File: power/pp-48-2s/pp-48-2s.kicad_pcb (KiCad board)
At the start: 4 copper layers, 150 x 95 mm, 178 parts, among them J1 BUS 40-60V, J101 NODE 1, J2 CTRL IN, J201 NODE 2, J3 CTRL OUT, J4 12V AUX OUT, J5 SWD, Q1 2N7002, Q101 BSC070N10NS5, Q102 2N7002, Q103 2N7002, Q104 2N7002, Q201 BSC070N10NS5, Q202 2N7002, Q203 2N7002, Q204 2N7002, U1 LM5164DDA, U101 LM5069MM-2, U102 INA238AIDGSR, U103 74LVC1G74, U104 TLP176AM, U105 TLP176AM, U106 TLP291, U2 LM5164DDA, U201 LM5069MM-2, U202 INA238AIDGSR, U203 74LVC1G74, U204 TLP176AM, U205 TLP176AM, U206 TLP291, U3 STM32G0B1CBT6, U4 ISO1640BD, U5 ISO7721D, U6 MCP23017-E/SO, X101 PM-19V-200W, X102 J2 AUX, X201 PM-19V-200W, X202 J2 AUX, Y1 8MHz

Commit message: power: syncfields ported to KiCad 10, PP-48-2S board fields synced from the schematic
FOOTPRINT.GetFieldByName is gone in KiCad 10; use HasField / GetField /
SetField by name. Description added to the synced fields, --dry option,
per-change report. Run on the board: 108 Value / LCSC / Description
fields on 174 footprints, kicad-cli drc --schematic-parity 0 mismatches
(was 104), copper untouched, DRC the same 5 warnings.
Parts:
- C22, C23: value 12p -> 33p
- J101: value NODE 1 -> NODE
- J201: value NODE 2 -> NODE

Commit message: power: PP-48-2S plane MCU STM32G0B1CBT6 -> STM32G070CBT6 (G0B1 out of stock at LCSC; pinout checked, 8-slot S7 pins moved off the unbonded 29/32); handoff: JLC stock check
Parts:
- U3: value STM32G0B1CBT6 -> STM32G070CBT6
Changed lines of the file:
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@@
 				(font
 					(size 1.27 1.27)
+					(thickness 0.15)
 				)
 			)
@@
 			)
 		)
-		(property "Value" "STM32G0B1CBT6"
+		(property "Value" "STM32G070CBT6"
 			(at 0 5.85 0)
 			(layer "F.Fab")
@@
 			)
 		)
-		(property "LCSC" "C2847904"
+		(property "LCSC" "C529338"
 			(at 0 0 0)
 			(layer "F.Fab")
@@
 			(layers "F.Cu" "F.Mask" "F.Paste")
 			(roundrect_rratio 0.25)
-			(net "unconnected-(U3-PA9{slash}UCPD1_DBCC1-Pad29)")
+			(net "unconnected-(U3-NC{slash}PA9-Pad29)")
 		)
 		(pad "30" smd roundrect
@@
 			(layers "F.Cu" "F.Mask" "F.Paste")
 			(roundrect_rratio 0.25)
-			(net "unconnected-(U3-PA10{slash}UCPD1_DBCC2-Pad32)")
+			(net "unconnected-(U3-NC{slash}PA10-Pad32)")
 		)
 		(pad "33" smd roundrect
@@
 				(font
 					(size 1.27 1.27)
+					(thickness 0.15)
 				)
 			)
@@
 				(font
 					(size 1.27 1.27)
+					(thickness 0.15)
 				)
 			)
@@
 				(font
 					(size 1.27 1.27)
+					(thickness 0.15)
 				)
 			)

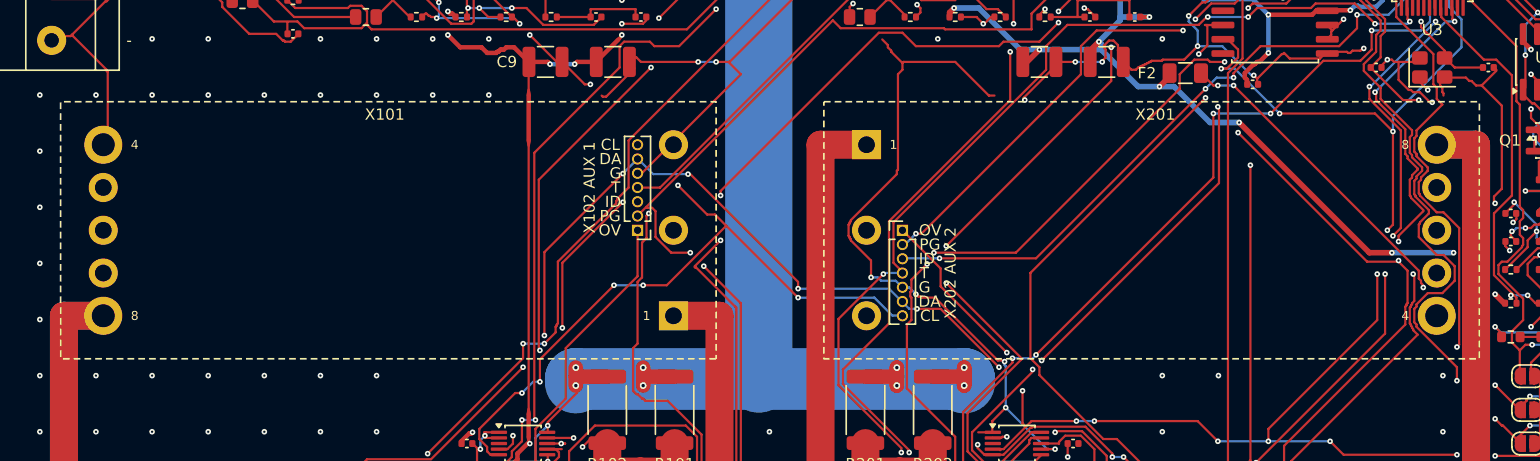
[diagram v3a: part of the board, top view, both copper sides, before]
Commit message: power: screwed PM module mount footprints (M2 into SMT standoffs, pogo aux) on module, plane and bench carrier; RUN moves to aux pad 8; copper not yet rerouted
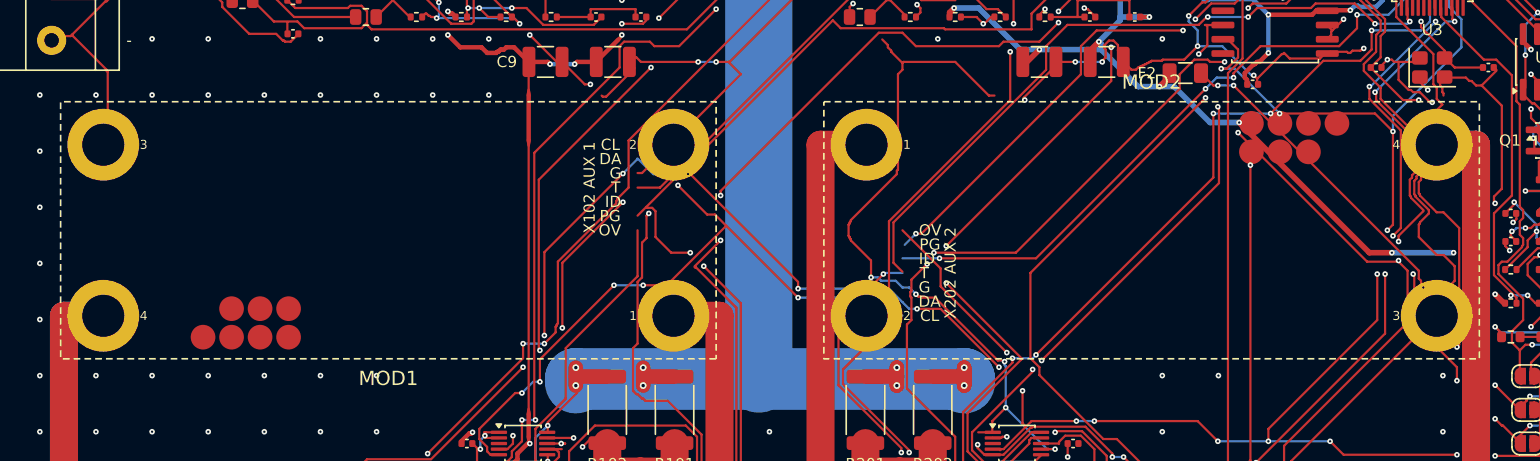
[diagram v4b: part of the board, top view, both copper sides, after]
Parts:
- removed X101, X201: PM-19V-200W, pp:Brick_Eighth_DOSA_Plane
- removed X102, X202: J2 AUX, Connector_PinHeader_1.27mm:PinHeader_1x07_P1.27mm_Vertical
- added MOD1: PM_Module_Outline, pp:PM_Module_Outline, F.Cu at (136.0, 137.0)
- added MOD2: PM_Module_Outline, pp:PM_Module_Outline, F.Cu at (204.0, 137.0)
- added PG101: pogo, pp:PM_Pogo_YZ130115073P, F.Cu at (127.1, 146.5)
- added PG102: pogo, pp:PM_Pogo_YZ130115073P, F.Cu at (124.6, 146.5)
- added PG103: pogo, pp:PM_Pogo_YZ130115073P, F.Cu at (122.0, 146.5)
- added PG104: pogo, pp:PM_Pogo_YZ130115073P, F.Cu at (119.5, 146.5)
- added PG105: pogo, pp:PM_Pogo_YZ130115073P, F.Cu at (127.1, 144.0)
- added PG106: pogo, pp:PM_Pogo_YZ130115073P, F.Cu at (124.6, 144.0)
- added PG107: pogo, pp:PM_Pogo_YZ130115073P, F.Cu at (122.0, 144.0)
- added PG201: pogo, pp:PM_Pogo_YZ130115073P, F.Cu at (212.9, 127.5)
- added PG202: pogo, pp:PM_Pogo_YZ130115073P, F.Cu at (215.4, 127.5)
- added PG203: pogo, pp:PM_Pogo_YZ130115073P, F.Cu at (218.0, 127.5)
- added PG204: pogo, pp:PM_Pogo_YZ130115073P, F.Cu at (220.5, 127.5)
- added PG205: pogo, pp:PM_Pogo_YZ130115073P, F.Cu at (212.9, 130.0)
- added PG206: pogo, pp:PM_Pogo_YZ130115073P, F.Cu at (215.4, 130.0)
- added PG207: pogo, pp:PM_Pogo_YZ130115073P, F.Cu at (218.0, 130.0)
- added SO101: M2x6 standoff, pp:PM_Standoff_M2x6_SMTSO, F.Cu at (161.4, 144.6)
- added SO102: M2x6 standoff, pp:PM_Standoff_M2x6_SMTSO, F.Cu at (161.4, 129.4)
- added SO103: M2x6 standoff, pp:PM_Standoff_M2x6_SMTSO, F.Cu at (110.6, 129.4)
- added SO104: M2x6 standoff, pp:PM_Standoff_M2x6_SMTSO, F.Cu at (110.6, 144.6)
- added SO201: M2x6 standoff, pp:PM_Standoff_M2x6_SMTSO, F.Cu at (178.6, 129.4)
- added SO202: M2x6 standoff, pp:PM_Standoff_M2x6_SMTSO, F.Cu at (178.6, 144.6)
- added SO203: M2x6 standoff, pp:PM_Standoff_M2x6_SMTSO, F.Cu at (229.4, 144.6)
- added SO204: M2x6 standoff, pp:PM_Standoff_M2x6_SMTSO, F.Cu at (229.4, 129.4)

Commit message: Revert "power: screwed PM module mount footprints (M2 into SMT standoffs, pogo aux) on module, plane and bench carrier; RUN moves to aux pad 8; copper not yet rerouted"
This reverts commit abb9f50ba34d0b63e5425fa3cd376420f2890e7d.
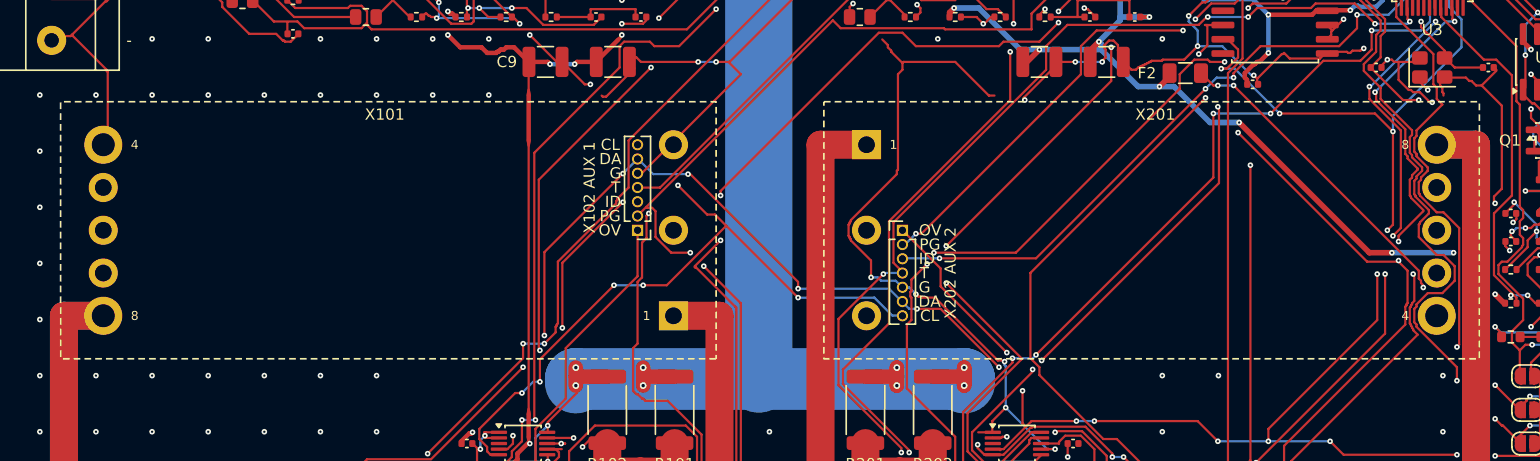
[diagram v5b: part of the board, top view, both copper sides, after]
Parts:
- removed MOD1, MOD2: PM_Module_Outline, pp:PM_Module_Outline
- removed PG101, PG102, PG103, PG104, PG105, PG106, PG107, PG201, PG202, PG203, PG204, PG205, PG206, PG207: pogo, pp:PM_Pogo_YZ130115073P
- removed SO101, SO102, SO103, SO104, SO201, SO202, SO203, SO204: M2x6 standoff, pp:PM_Standoff_M2x6_SMTSO
- added X101: PM-19V-200W, pp:Brick_Eighth_DOSA_Plane, F.Cu at (136.0, 137.0)
- added X102: J2 AUX, Connector_PinHeader_1.27mm:PinHeader_1x07_P1.27mm_Vertical, F.Cu at (158.2, 137.0)
- added X201: PM-19V-200W, pp:Brick_Eighth_DOSA_Plane, F.Cu at (204.0, 137.0)
- added X202: J2 AUX, Connector_PinHeader_1.27mm:PinHeader_1x07_P1.27mm_Vertical, F.Cu at (181.8, 137.0)
